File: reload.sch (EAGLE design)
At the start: 23 parts, among them IC1 OPAMP-DUALMS, IC2 V_REG_MIC2920, Q1 BTS117, Q2 BTS117

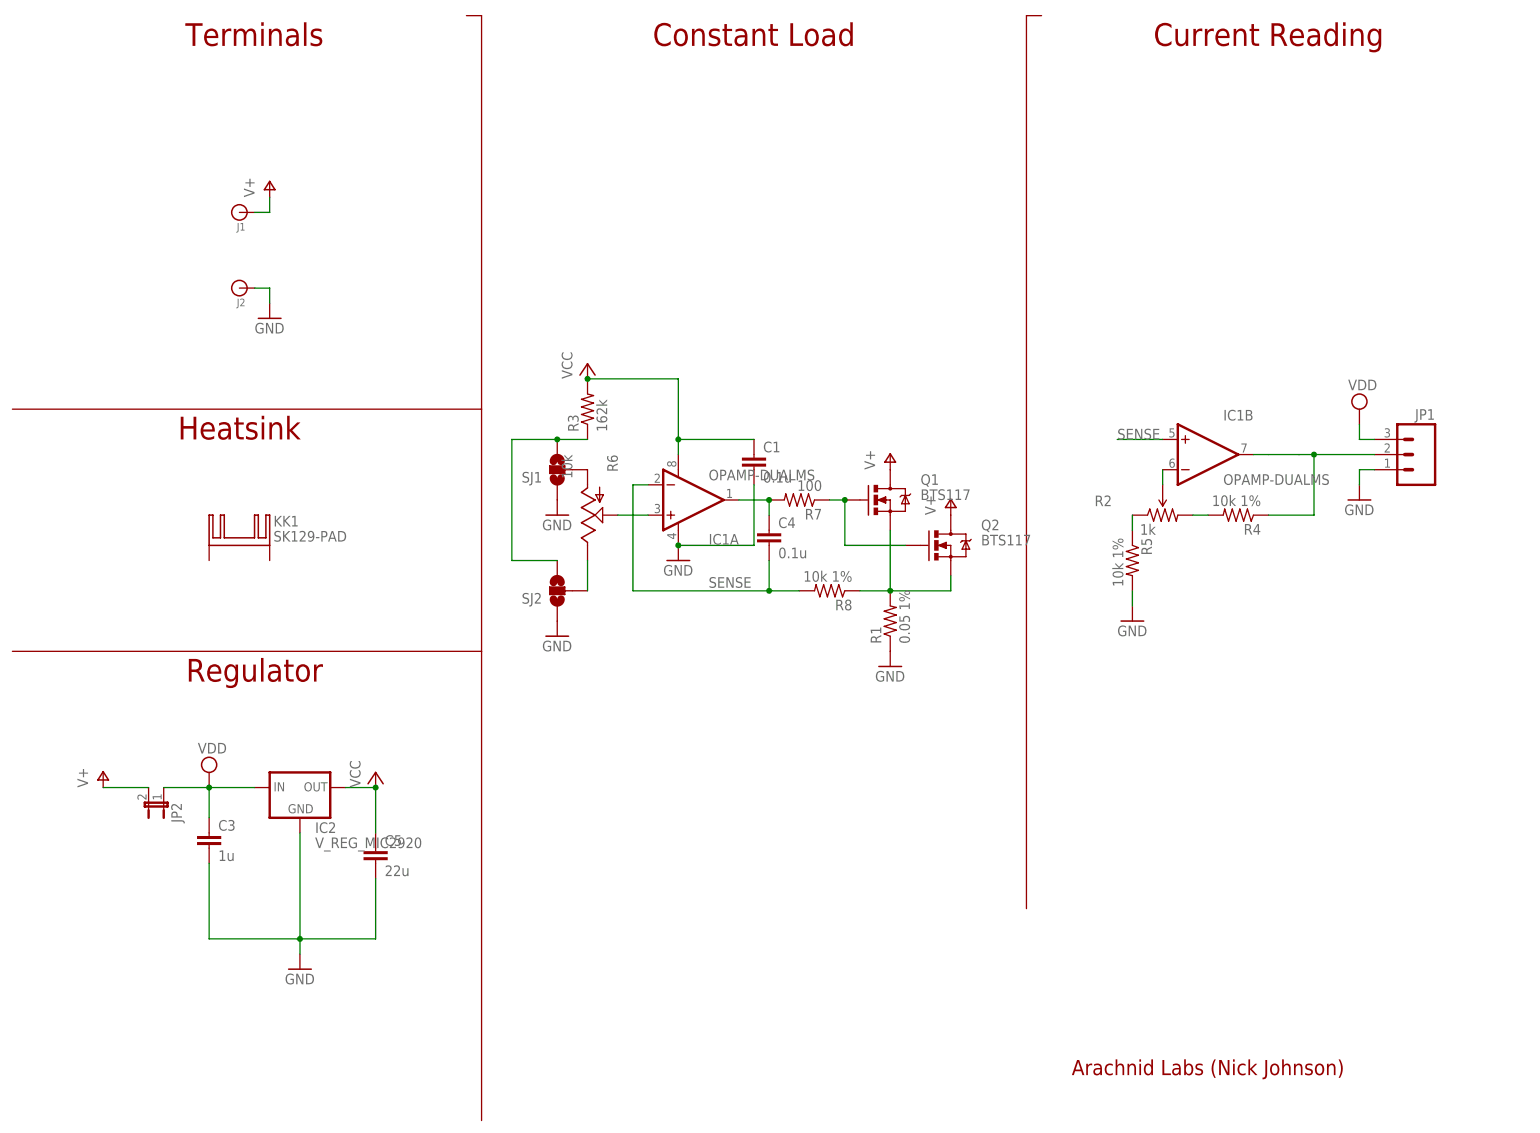
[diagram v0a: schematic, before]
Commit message: change components and layout
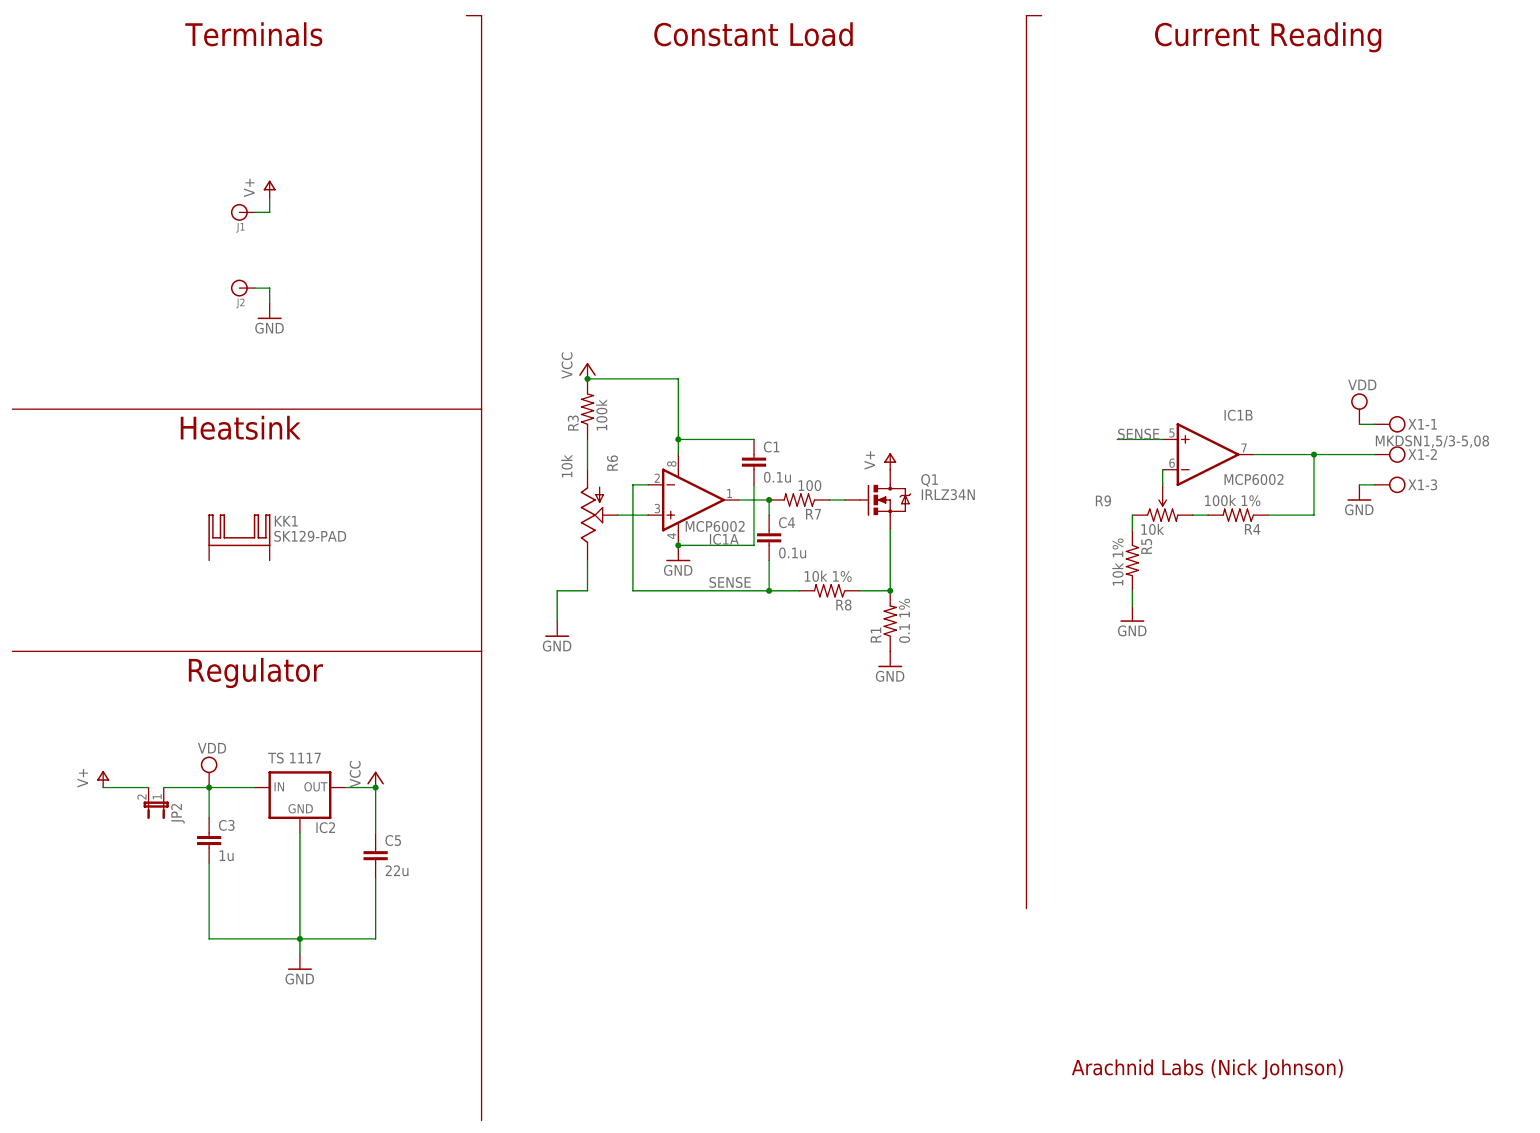
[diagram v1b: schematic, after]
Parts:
- removed JP1: (no value), SparkFun-Connectors:M031X03_NO_SILK
- removed Q2: BTS117, SparkFun-DiscreteSemi:MOSFET-NCHANNELPTH2
- removed R2: 1k, nickparts:TRIMPOT3MM-2
- removed SJ1: (no value), SparkFun-Passives:SOLDERJUMPER_2WAYPASTE2&3
- removed SJ2: (no value), SparkFun-Passives:SOLDERJUMPER_2WAYPASTE1&2
- added R9: 10k, trimmer:TRIMPOTTS53YJ
- added X1: MKDSN1,5/3-5,08, con-phoenix-508:MKDSN1,5/3-5,08
- IC1: value OPAMP-DUALMS -> MCP6002
- IC2: value V_REG_MIC2920 -> TS 1117
- JP2: device SparkFun-Passives:JUMPER-2SMD-NC -> SparkFun-Passives:JUMPER-2PTH
- Q1: value BTS117 -> IRLZ34N
- R1: value 0.05 1% -> 0.1 1%
- R3: value 162k -> 100k
- R4: value 10k 1% -> 100k 1%
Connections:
- removed net N$10: R3.1, SJ1.3, SJ2.3
- removed net N$8: R6.E, SJ2.2
- net GND: now also R6.E, X1-3.KL; no longer JP1.1, SJ1.1, SJ2.1
- net IREF: now also X1-2.KL; no longer JP1.2
- net N$2: now also R3.1; no longer SJ1.2
- net N$3: no longer Q2.S
- net N$5: now also R9.WIPER; no longer R2.WIPER
- net N$6: now also R9.CCW; no longer R2.CCW
- net N$7: now also R9.CW; no longer R2.CW
- net N$9: no longer Q2.G
- net V+: no longer Q2.D
- net VDD: now also X1-1.KL; no longer JP1.3

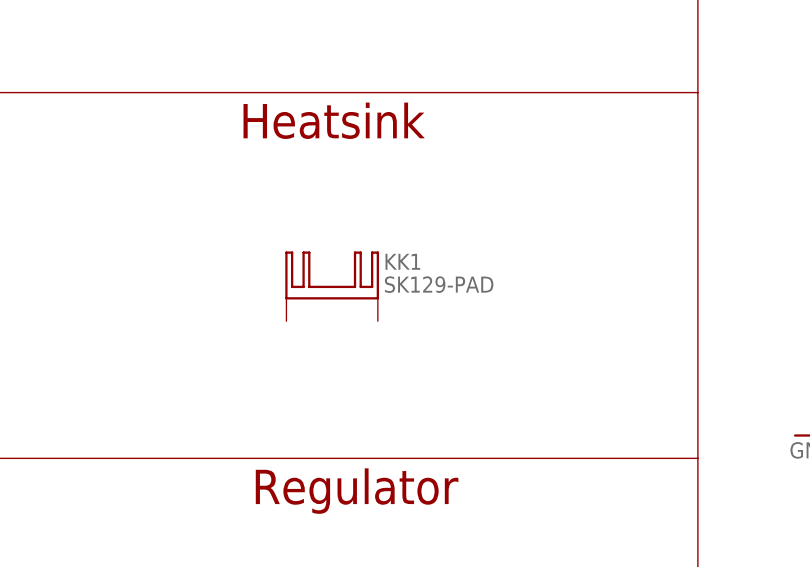
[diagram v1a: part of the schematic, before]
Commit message: Delete heatsink for panelize
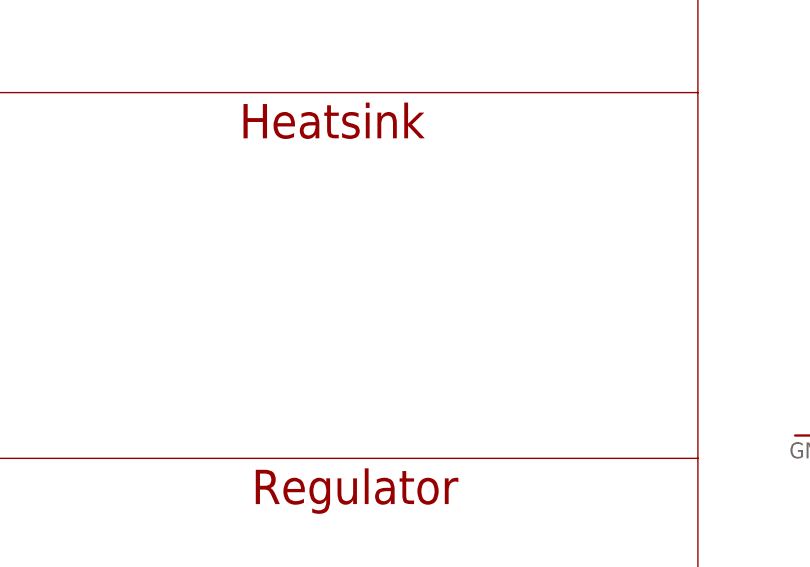
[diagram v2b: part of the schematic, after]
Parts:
- removed KK1: SK129-PAD, nickparts:SK129-PAD
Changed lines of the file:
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@@
 <?xml version="1.0" encoding="utf-8"?>
 <!DOCTYPE eagle SYSTEM "eagle.dtd">
-<eagle version="6.3">
+<eagle version="6.6.0">
 <drawing>
 <settings>
@@
 <part name="GND7" library="supply1" deviceset="GND" device=""/>
 <part name="C3" library="SparkFun-Passives" deviceset="CAP" device="0805" value="1u"/>
-<part name="KK1" library="nickparts" deviceset="SK129-PAD" device=""/>
 <part name="R7" library="SparkFun-Passives" deviceset="RESISTOR" device="0805-RES" value="100"/>
 <part name="P+2" library="supply1" deviceset="VCC" device=""/>
@@
 <instance part="GND7" gate="1" x="43.18" y="134.62"/>
 <instance part="C3" gate="G$1" x="33.02" y="45.72"/>
-<instance part="KK1" gate="G$1" x="38.1" y="96.52"/>
 <instance part="R7" gate="G$1" x="132.08" y="104.14" rot="R180"/>
 <instance part="P+2" gate="VCC" x="60.96" y="58.42"/>

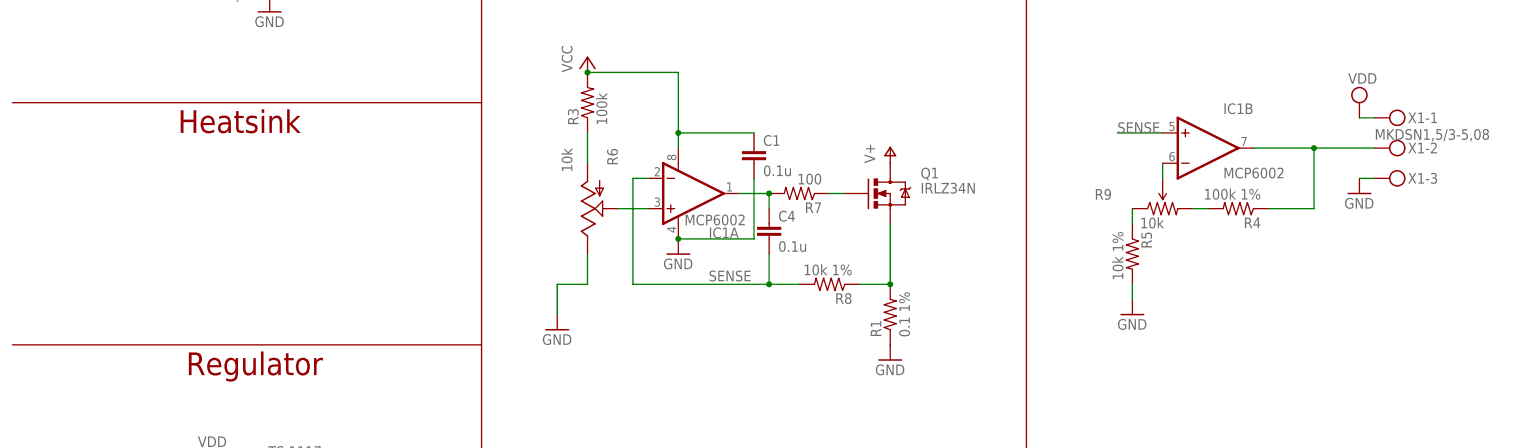
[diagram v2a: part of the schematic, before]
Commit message: rearrange part identifiers for silkscreen change bottom ground plane
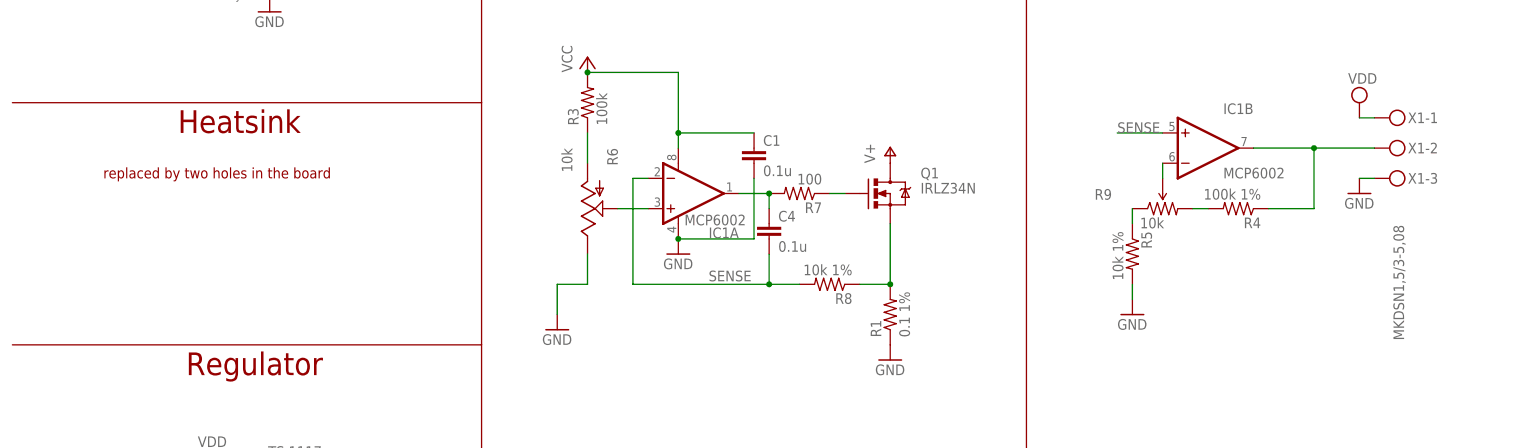
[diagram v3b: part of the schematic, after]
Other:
- note added: "replaced by two holes in the board"
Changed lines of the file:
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@@
 <text x="210.82" y="180.34" size="3.81" layer="94" align="bottom-center">Current Reading</text>
 <text x="200.66" y="7.62" size="2.54" layer="94" align="bottom-center">Arachnid Labs (Nick Johnson)</text>
+<text x="15.24" y="106.68" size="1.778" layer="94">replaced by two holes in the board</text>
 </plain>
 <instances>
@@
 <instance part="SUPPLY2" gate="G$1" x="226.06" y="119.38"/>
 <instance part="C5" gate="G$1" x="60.96" y="43.18"/>
-<instance part="X1" gate="-1" x="231.14" y="116.84"/>
+<instance part="X1" gate="-1" x="231.14" y="116.84" smashed="yes">
+<attribute name="NAME" x="234.188" y="115.951" size="1.778" layer="95"/>
+<attribute name="VALUE" x="233.553" y="79.502" size="1.778" layer="96" rot="R90"/>
+</instance>
 <instance part="X1" gate="-2" x="231.14" y="111.76"/>
 <instance part="X1" gate="-3" x="231.14" y="106.68"/>
